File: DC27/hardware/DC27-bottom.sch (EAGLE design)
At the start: 95 parts, among them IC2 LDL112D33R, IC3 FT2232HL-REEL, IC4 93LC46BT-I_OT, J1 PAIRING, J2 JTAG, J3 Battery, J4 Program Port, U2 ESP-WROOM-32, Y1 ABM7-12.000MHZ-D2Y-T

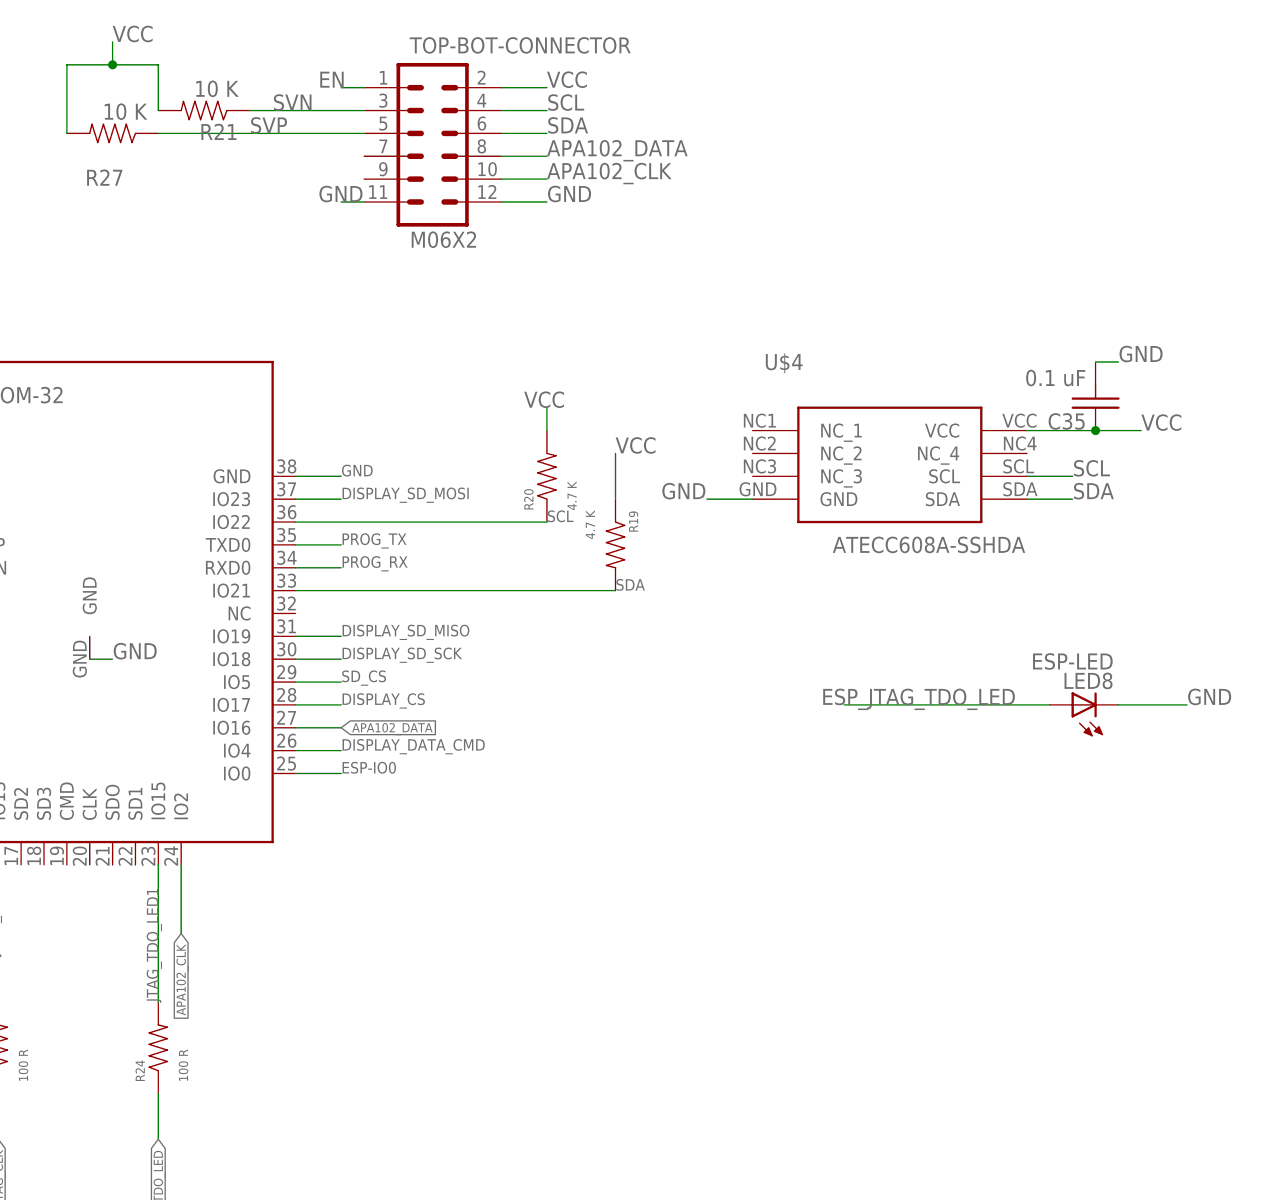
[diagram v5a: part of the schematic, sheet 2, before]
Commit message: final tweaks moved top board I2C to separate bus
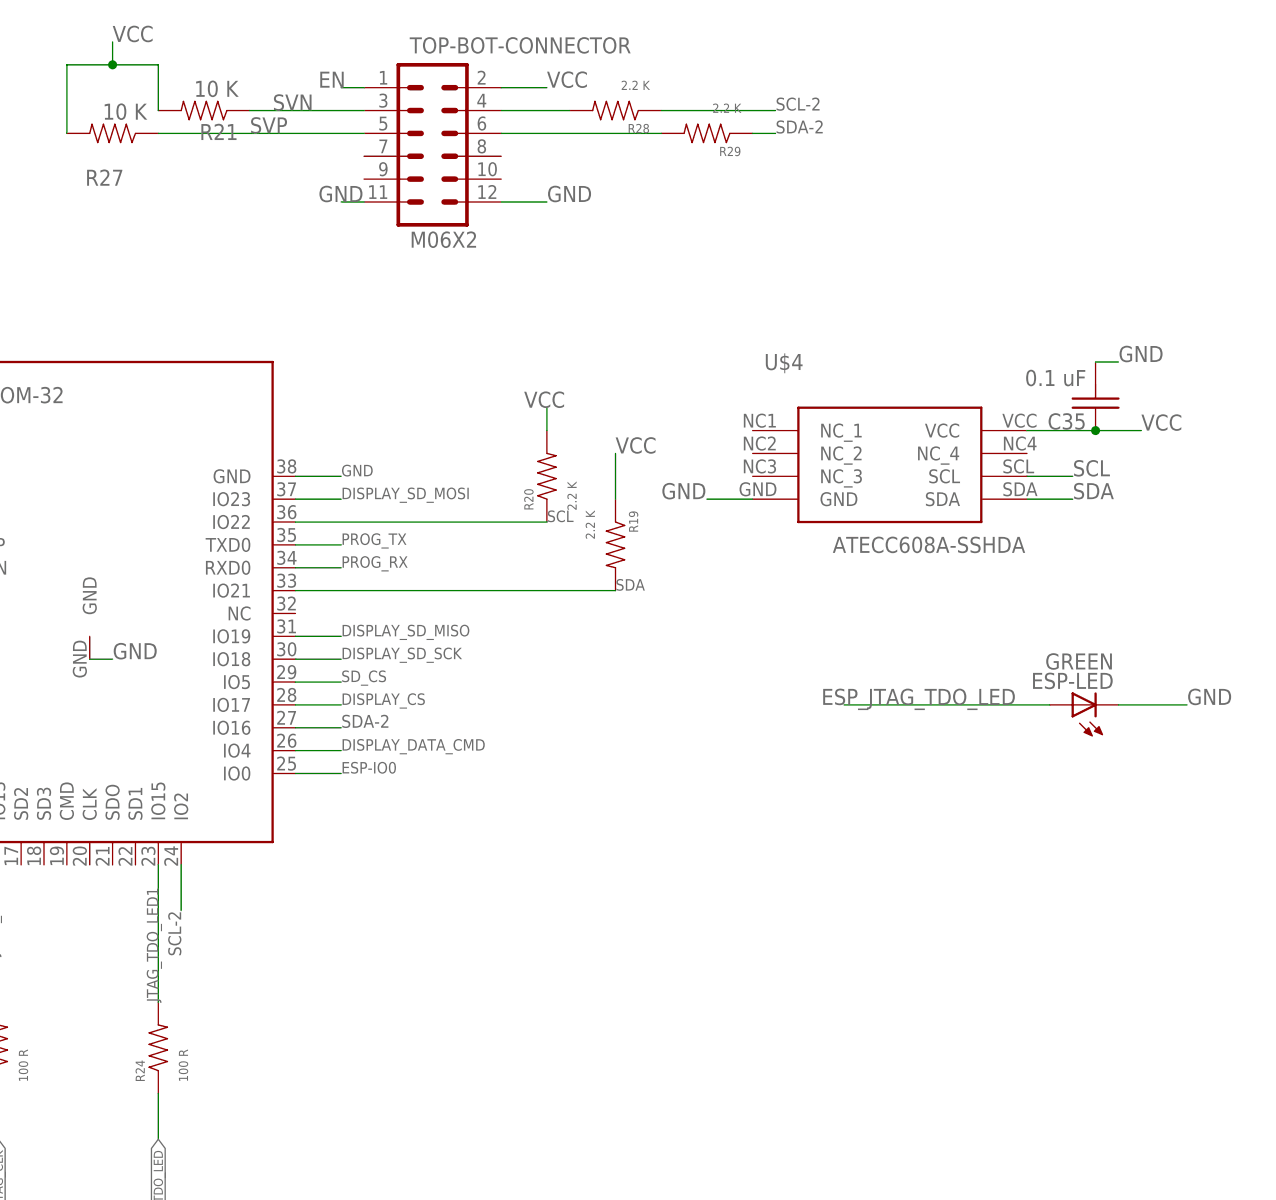
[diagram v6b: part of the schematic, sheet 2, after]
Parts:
- added R28, R29: 2.2 K, dc-26:RESISTOR0805-RES
- CL1: value cl1 -> BLUE
- CL2: value cl2 -> BLUE
- CL3: value cl3 -> BLUE
- CL4: value cl4 -> BLUE
- ESP-LED: value ESP-LED -> GREEN
- KEYLED: value KeyLed -> GREEN
- R19, R20: value 4.7 K -> 2.2 K
- RX-LED: value rx-led -> BLUE
- TX-LED: value tx-led -> GREEN
- renumbered LED1 to CL1, LED2 to RX-LED, LED3 to TX-LED, LED4 to CL2, LED5 to CL3, LED6 to CL4, LED7 to KEYLED, LED8 to ESP-LED
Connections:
- removed net APA102_CLK: TOP-BOT-CONNECTOR.10, U2.IO2
- removed net APA102_DATA: TOP-BOT-CONNECTOR.8, U2.IO16
- new net N$1: R28.2, TOP-BOT-CONNECTOR.4
- new net N$2: R29.2, TOP-BOT-CONNECTOR.6
- new net SCL-2: R28.1, U2.IO2
- new net SDA-2: R29.1, U2.IO16
- net SCL: no longer TOP-BOT-CONNECTOR.4
- net SDA: no longer TOP-BOT-CONNECTOR.6

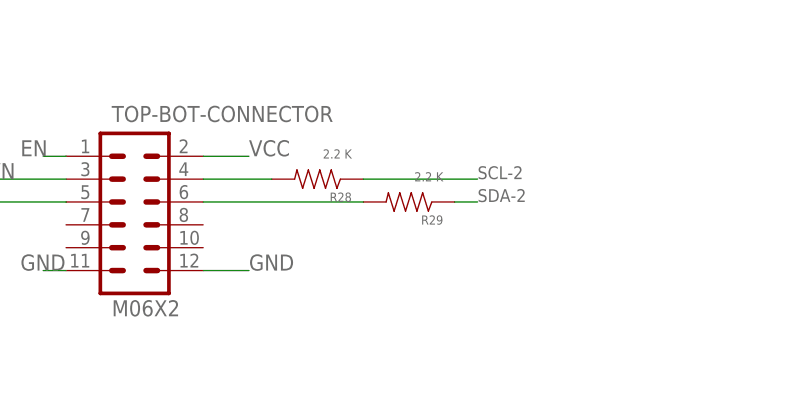
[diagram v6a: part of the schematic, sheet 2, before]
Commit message: fixed i2c pull ups to be actual pull ups
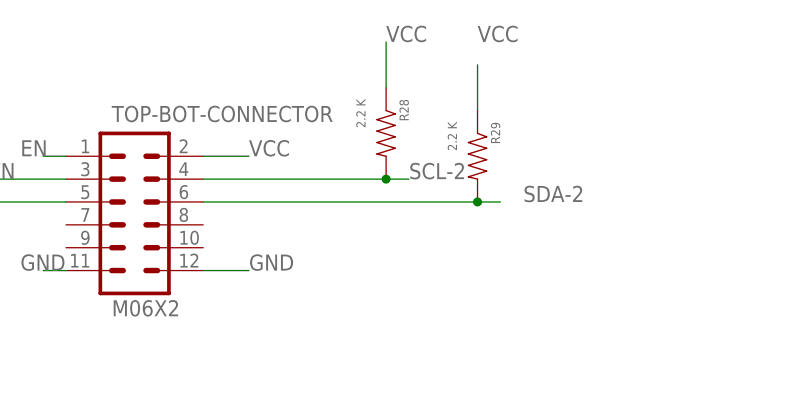
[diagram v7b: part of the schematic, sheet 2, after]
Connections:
- removed net N$1: R28.2, TOP-BOT-CONNECTOR.4
- removed net N$2: R29.2, TOP-BOT-CONNECTOR.6
- net SCL-2: now also R28.2, TOP-BOT-CONNECTOR.4; no longer R28.1
- net SDA-2: now also R29.2, TOP-BOT-CONNECTOR.6; no longer R29.1
- net VCC: now also R28.1, R29.1
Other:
- moved on the sheet: R28, R29
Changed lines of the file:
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@@
 <attribute name="VALUE" x="118.11" y="130.302" size="1.778" layer="96" rot="R180"/>
 </instance>
-<instance part="R28" gate="G$1" x="170.18" y="129.54" smashed="yes" rot="R180">
-<attribute name="NAME" x="173.99" y="128.0414" size="1.016" layer="95" rot="R180"/>
-<attribute name="VALUE" x="173.99" y="132.842" size="1.016" layer="96" rot="R180"/>
+<instance part="R28" gate="G$1" x="177.8" y="134.62" smashed="yes" rot="R270">
+<attribute name="NAME" x="179.2986" y="138.43" size="1.016" layer="95" rot="R270"/>
+<attribute name="VALUE" x="174.498" y="138.43" size="1.016" layer="96" rot="R270"/>
 </instance>
-<instance part="R29" gate="G$1" x="180.34" y="127" smashed="yes" rot="R180">
-<attribute name="NAME" x="184.15" y="125.5014" size="1.016" layer="95" rot="R180"/>
-<attribute name="VALUE" x="184.15" y="130.302" size="1.016" layer="96" rot="R180"/>
+<instance part="R29" gate="G$1" x="187.96" y="132.08" smashed="yes" rot="R270">
+<attribute name="NAME" x="189.4586" y="135.89" size="1.016" layer="95" rot="R270"/>
+<attribute name="VALUE" x="184.658" y="135.89" size="1.016" layer="96" rot="R270"/>
 </instance>
 </instances>
@@
 <label x="114.3" y="137.16" size="1.778" layer="95"/>
 </segment>
+<segment>
+<pinref part="R28" gate="G$1" pin="1"/>
+<wire x1="177.8" y1="139.7" x2="177.8" y2="144.78" width="0.1524" layer="91"/>
+<label x="177.8" y="144.78" size="1.778" layer="95"/>
+</segment>
+<segment>
+<pinref part="R29" gate="G$1" pin="1"/>
+<wire x1="187.96" y1="137.16" x2="187.96" y2="142.24" width="0.1524" layer="91"/>
+<label x="187.96" y="144.78" size="1.778" layer="95"/>
+</segment>
 </net>
 <net name="GND" class="0">
@@
 </segment>
 <segment>
-<pinref part="R28" gate="G$1" pin="1"/>
-<wire x1="175.26" y1="129.54" x2="187.96" y2="129.54" width="0.1524" layer="91"/>
-<label x="187.96" y="129.54" size="1.4224" layer="95"/>
+<pinref part="TOP-BOT-CONNECTOR" gate="G$1" pin="4"/>
+<wire x1="157.48" y1="129.54" x2="177.8" y2="129.54" width="0.1524" layer="91"/>
+<pinref part="R28" gate="G$1" pin="2"/>
+<wire x1="177.8" y1="129.54" x2="180.34" y2="129.54" width="0.1524" layer="91"/>
+<junction x="177.8" y="129.54"/>
+<label x="180.34" y="129.54" size="1.778" layer="95"/>
 </segment>
 </net>
@@
 </segment>
 <segment>
-<pinref part="R29" gate="G$1" pin="1"/>
-<wire x1="185.42" y1="127" x2="187.96" y2="127" width="0.1524" layer="91"/>
-<label x="187.96" y="127" size="1.4224" layer="95"/>
-</segment>
-</net>
-<net name="N$1" class="0">
-<segment>
-<pinref part="TOP-BOT-CONNECTOR" gate="G$1" pin="4"/>
-<wire x1="157.48" y1="129.54" x2="165.1" y2="129.54" width="0.1524" layer="91"/>
-<pinref part="R28" gate="G$1" pin="2"/>
-</segment>
-</net>
-<net name="N$2" class="0">
-<segment>
 <pinref part="TOP-BOT-CONNECTOR" gate="G$1" pin="6"/>
-<wire x1="157.48" y1="127" x2="175.26" y2="127" width="0.1524" layer="91"/>
+<wire x1="157.48" y1="127" x2="187.96" y2="127" width="0.1524" layer="91"/>
 <pinref part="R29" gate="G$1" pin="2"/>
-</segment>
-</net>
+<wire x1="187.96" y1="127" x2="190.5" y2="127" width="0.1524" layer="91"/>
+<junction x="187.96" y="127"/>
+<label x="193.04" y="127" size="1.778" layer="95"/>
+</segment>
+</net>
